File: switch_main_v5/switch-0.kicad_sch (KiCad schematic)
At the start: 43 parts, among them U902 SJA1105QELY, Y902 XRCGB25M000F3A16R0

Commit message: Updated 1v0_buck_converter feedback resistors
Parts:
- removed C937, C938, C939, C941, C942, C943, C944, C945, C961, C967: 1u, Capacitor_SMD:C_0402_1005Metric, symbol Device:C_Small
- removed C940, C946, C947, C948, C949, C950, C951, C952, C953, C954, C955, C956, C957, C958, C959, C960, C962, C963, C964, C965, C966, C968, C969, C970: 100n, Capacitor_SMD:C_0402_1005Metric, symbol Device:C_Small
- removed R904, R906: 10k, Resistor_SMD:R_0402_1005Metric, symbol Device:R_Small
- removed R905: 22R, Resistor_SMD:R_0402_1005Metric, symbol Device:R_Small
- removed TP903, TP904: 1.5mm, TestPoint:TestPoint_Pad_D1.5mm, symbol Connector:TestPoint_Small
- removed U902: SJA1105QELY, project_footprints:BGA159C80P14X14_1200X1200X150, symbol ETH-SWCH:SJA1105QELY
- added C901, C902, C903, C905, C906, C907, C908, C909, C925, C931: 1u, Capacitor_SMD:C_0402_1005Metric, symbol Device:C_Small
- added C904, C910, C911, C912, C913, C914, C915, C916, C917, C918, C919, C920, C921, C922, C923, C924, C926, C927, C928, C929, C930, C932, C933, C934: 100n, Capacitor_SMD:C_0402_1005Metric, symbol Device:C_Small
- added R901, R903: 10k, Resistor_SMD:R_0402_1005Metric, symbol Device:R_Small
- added R902: 22R, Resistor_SMD:R_0402_1005Metric, symbol Device:R_Small
- added TP901, TP902: 1.5mm, TestPoint:TestPoint_Pad_D1.5mm, symbol Connector:TestPoint_Small
- added U901: SJA1105QELY, project_footprints:BGA159C80P14X14_1200X1200X150, symbol ETH-SWCH:SJA1105QELY
- renumbered C971 to C935, C972 to C936, Y902 to Y901
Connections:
- net +1V2: now also C901.1, C903.1, C904.1, C911.1, C912.1, C919.1, C925.1, C926.1, C927.1, C928.1, C929.1, C930.1, C932.1, U901.D6 (VDD_CORE_1), U901.D9 (VDD_CORE_2), U901.F11 (VDD_CORE_4), U901.F4 (VDD_CORE_3), U901.J1 (VDDA_PLL), U901.J11 (VDD_CORE_6), U901.J4 (VDD_CORE_5), U901.K1 (VDDA_OSC), U901.L6 (VDD_CORE_7), U901.L9 (VDD_CORE_8)
- net +1V8: now also C905.1, C906.1, C907.1, C913.1, C914.1, C915.1, C920.1, C921.1, C922.1, C931.1, C933.1, C934.1, U901.D10 (VDDIO_MII2_1), U901.D11 (VDDIO_MII2_2), U901.D4 (VDDIO_MII0_1), U901.D5 (VDDIO_MII1_1), U901.D7 (VDDIO_MII1_2), U901.D8 (VDDIO_MII1_3), U901.E11 (VDDIO_MII2_3), U901.E4 (VDDIO_MII0_2), U901.G4 (VDDIO_MII0_3), U901.H4 (VDDIO_CLO)
- net +3V3: now also C902.1, C908.1, C909.1, C910.1, C916.1, C917.1, C918.1, C923.1, C924.1, R901.2, R903.2, U901.G11 (VDDIO_MII3_1), U901.H11 (VDDIO_MII3_2), U901.K11 (VDDIO_MII3_3), U901.L10 (VDDIO_MII4_2), U901.L11 (VDDIO_MII4_3), U901.L5 (VDDIO_HOST), U901.L8 (VDDIO_MII4_1)
- net CLK: now also U901.P5 (SCK)
- net CLK_OUT: now also R902.1
- net CS: now also R901.1, U901.N6 (SS_N)
- net GND1: now also C901.2, C902.2, C903.2, C904.2, C905.2, C906.2, C907.2, C908.2, C909.2, C910.2, C911.2, C912.2, C913.2, C914.2, C915.2, C916.2, C917.2, C918.2, C919.2, C920.2, C921.2, C922.2, C923.2, C924.2, C925.2, C926.2, C927.2, C928.2, C929.2, C930.2, C931.2, C932.2, C933.2, C934.2, TP901.1, U901.A1 (VSS_1), U901.A14 (VSS_2), U901.B10 (MII2_RX_ER), U901.B13 (VSS_3), U901.B3 (MII1_RX_ER), U901.E10 (VSS_9), U901.E5 (VSS_4), U901.E6 (VSS_5), U901.E7 (VSS_6), U901.E8 (VSS_7), U901.E9 (VSS_8), U901.F10 (VSS_15), U901.F5 (VSS_10), U901.F6 (VSS_11), U901.F7 (VSS_12), U901.F8 (VSS_13), U901.F9 (VSS_14), U901.G10 (VSS_21), U901.G13 (MII3_RXD3), U901.G5 (VSS_16), U901.G6 (VSS_17), U901.G7 (VSS_18), U901.G8 (VSS_19), U901.G9 (VSS_20), U901.H10 (VSS_27), U901.H14 (MII3_RXD2), U901.H2 (MII0_RX_ER), U901.H5 (VSS_22), U901.H6 (VSS_23), U901.H7 (VSS_24), U901.H8 (VSS_25), U901.H9 (VSS_26), U901.J10 (VSS_33), U901.J13 (MII3_RX_CLK/RXC), U901.J2 (VSSA_PLL), U901.J5 (VSS_28), U901.J6 (VSS_29), U901.J7 (VSS_30), U901.J8 (VSS_31), U901.J9 (VSS_32), U901.K10 (VSS_40), U901.K4 (VSS_34), U901.K5 (VSS_35), U901.K6 (VSS_36), U901.K7 (VSS_37), U901.K8 (VSS_38), U901.K9 (VSS_39), U901.L2 (VSSA_OSC), U901.L4 (I.C.), U901.L7 (VSS_41), U901.N11 (MII4_RXD2), U901.N13 (VSS_43), U901.N2 (VSS_42), U901.P1 (VSS_44), U901.P10 (MII4_RX_CLK/RXC), U901.P12 (MII4_RXD3), U901.P13 (MII4_RX_ER), U901.P14 (VSS_45)
- net MISO: now also U901.P4 (SDO)
- net MOSI: now also U901.N5 (SDI)
- net OSC_IN: now also U901.K2 (OSC_IN)
- net OSC_OUT: now also U901.L1 (OSC_OUT)
- net PTP_CLK: now also U901.N4 (PTP_CLK)
- net R_{CLK_OUT}: now also R902.2, U901.H1 (CLK_OUT)
- net xMII0.RX_CLK: now also U901.E2 (MII0_RX_CLK/RXC)
- net xMII0.RX_CTL: now also U901.G1 (MII0_RX_DV/CRS_DV/RX_CTL)
- net xMII0.RX_D0: now also U901.E1 (MII0_RXD0)
- net xMII0.RX_D1: now also U901.F2 (MII0_RXD1)
- net xMII0.RX_D2: now also U901.F1 (MII0_RXD2)
- net xMII0.RX_D3: now also U901.G2 (MII0_RXD3)
- net xMII0.TX_CLK: now also U901.D1 (MII0_TX_CLK/REF_CLK/TXC)
- net xMII0.TX_CTL: now also U901.D2 (MII0_TX_EN/TX_CTL)
- net xMII0.TX_D0: now also U901.A2 (MII0_TXD0)
- net xMII0.TX_D1: now also U901.B1 (MII0_TXD1)
- net xMII0.TX_D2: now also U901.C2 (MII0_TXD2)
- net xMII0.TX_D3: now also U901.C1 (MII0_TXD3)
- net xMII1.RX_CLK: now also U901.B6 (MII1_RX_CLK/RXC)
- net xMII1.RX_CTL: now also U901.A4 (MII1_RX_DV/CRS_DV/RX_CTL)
- net xMII1.RX_D0: now also U901.A6 (MII1_RXD0)
- net xMII1.RX_D1: now also U901.B5 (MII1_RXD1)
- net xMII1.RX_D2: now also U901.A5 (MII1_RXD2)
- net xMII1.RX_D3: now also U901.B4 (MII1_RXD3)
- net xMII1.TX_CLK: now also U901.A7 (MII1_TX_CLK/REF_CLK/TXC)
- net xMII1.TX_CTL: now also U901.B7 (MII1_TTX_EN/TX_CTL)
- net xMII1.TX_D0: now also U901.B9 (MII1_TXD0)
- net xMII1.TX_D1: now also U901.A9 (MII1_TXD1)
- net xMII1.TX_D2: now also U901.B8 (MII1_TXD2)
- net xMII1.TX_D3: now also U901.A8 (MII1_TXD3)
- net xMII2.RX_CLK: now also U901.B14 (MII2_RX_CLK/RXC)
- net xMII2.RX_CTL: now also U901.A11 (MII2_RX_DV/CRS_DV/RX_CTL)
- net xMII2.RX_D0: now also U901.A13 (MII2_RXD0)
- net xMII2.RX_D1: now also U901.B12 (MII2_RXD1)
- net xMII2.RX_D2: now also U901.A12 (MII2_RXD2)
- net xMII2.RX_D3: now also U901.B11 (MII2_RXD3)
- net xMII2.TX_CLK: now also U901.C14 (MII2_TX_CLK/REF_CLK/TXC)
- net xMII2.TX_CTL: now also U901.C13 (MII2_TX_EN/TX_CTL)
- net xMII2.TX_D0: now also U901.E13 (MII2_TXD0)
- net xMII2.TX_D1: now also U901.E14 (MII2_TXD1)
- net xMII2.TX_D2: now also U901.D13 (MII2_TXD2)
- net xMII2.TX_D3: now also U901.D14 (MII2_TXD3)
- net xMII3.RX_CRS_DV: now also U901.G14 (MII3_RX_DV/CRS_DV/RX_CTL)
- net xMII3.RX_D0: now also U901.J14 (MII3_RXD0)
- net xMII3.RX_D1: now also U901.H13 (MII3_RXD1)
- net xMII3.RX_ER: now also U901.F13 (MII3_RX_ER)
- net xMII3.TX_D0: now also U901.M13 (MII3_TXD0)
- net xMII3.TX_D1: now also U901.M14 (MII3_TXD1)
- net xMII3.TX_EN: now also U901.K13 (MII3_TX_EN/TX_CTL)
- net xMII3_REF_CLK: now also U901.K14 (MII3_TX_CLK/REF_CLK/TXC)
- net xMII4.RX_CRS_DV: now also U901.P9 (MII4_TX_EN/TX_CTL)
- net xMII4.RX_D0: now also U901.P7 (MII4_TXD0)
- net xMII4.RX_D1: now also U901.N7 (MII4_TXD1)
- net xMII4.TX_D0: now also U901.N10 (MII4_RXD0)
- net xMII4.TX_D1: now also U901.P11 (MII4_RXD1)
- net xMII4.TX_EN: now also U901.N12 (MII4_RX_DV/CRS_DV/RX_CTL)
- net xMII4_REF_CLK: now also U901.N9 (MII4_TX_CLK/REF_CLK/TXC)
- net ~{RST}: now also R903.1, TP902.1, U901.P3 (RST_N)

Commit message: Placed most remaining passives and test points
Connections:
- net CS renamed SS
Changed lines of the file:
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@@
-		)
-	)
-	(label "CS"
-		(at 228.6 121.92 0)
-		(effects
-			(font
-				(size 1.27 1.27)
-			)
-			(justify left bottom)
 		)
 	)
@@
 		)
 	)
-	(hierarchical_label "CS"
-		(shape input)
-		(at 220.98 121.92 180)
-		(effects
-			(font
-				(size 1.27 1.27)
-			)
-			(justify right)
-		)
-	)
 	(hierarchical_label "xMII4_REF_CLK"
 		(shape output)
@@
 		)
 	)
+	(hierarchical_label "SS"
+		(shape input)
+		(at 220.98 121.92 180)
+		(effects
+			(font
+				(size 1.27 1.27)
+			)
+			(justify right)
+		)
+	)

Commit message: Tidied schematic and PCB
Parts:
- renumbered C901 to C1501, C904 to C1502, C912 to C1503, C919 to C1504, C926 to C1505, C928 to C1506, C929 to C1507, C930 to C1508, C932 to C1509, C905 to C1510, C913 to C1511, C920 to C1512, C906 to C1513, C914 to C1514, C921 to C1515, C907 to C1516, C915 to C1517, C922 to C1518, C935 to C1519, C908 to C1520, C916 to C1521, C923 to C1522, C936 to C1523, C909 to C1524, C917 to C1525, C924 to C1526, C902 to C1527, C910 to C1528, C918 to C1529, C903 to C1530, C911 to C1531, C925 to C1532, C927 to C1533, C931 to C1534, C933 to C1535, C934 to C1536, R901 to R1501, R903 to R1502, R902 to R1503, TP901 to TP1501, TP902 to TP1502, U901 to U1501, Y901 to Y1501

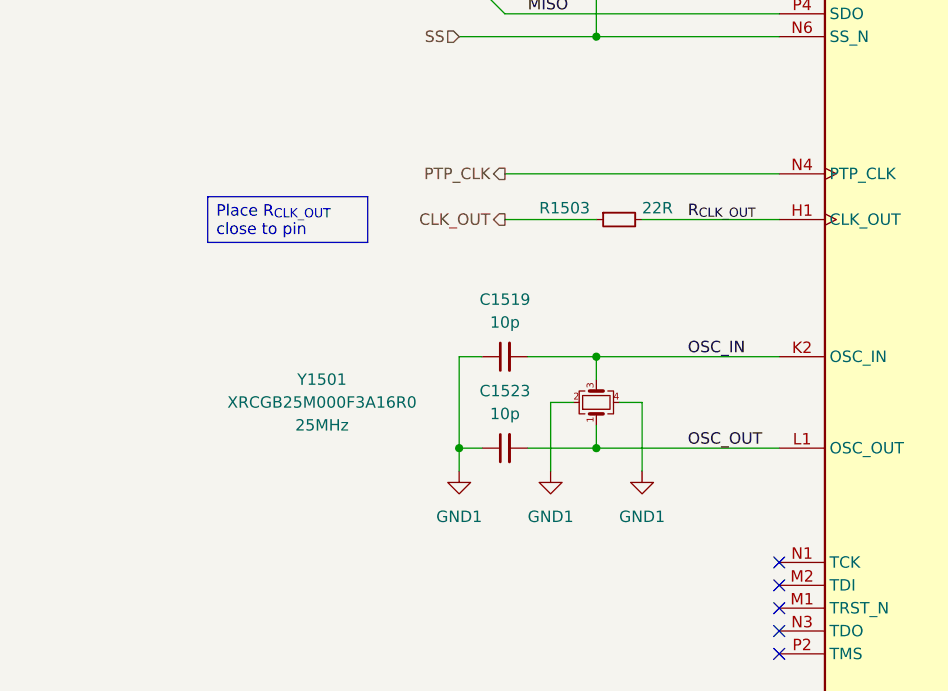
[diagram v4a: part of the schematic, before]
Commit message: Removed one switch crystal so both are now clocked from the same source and timestamps won't drift
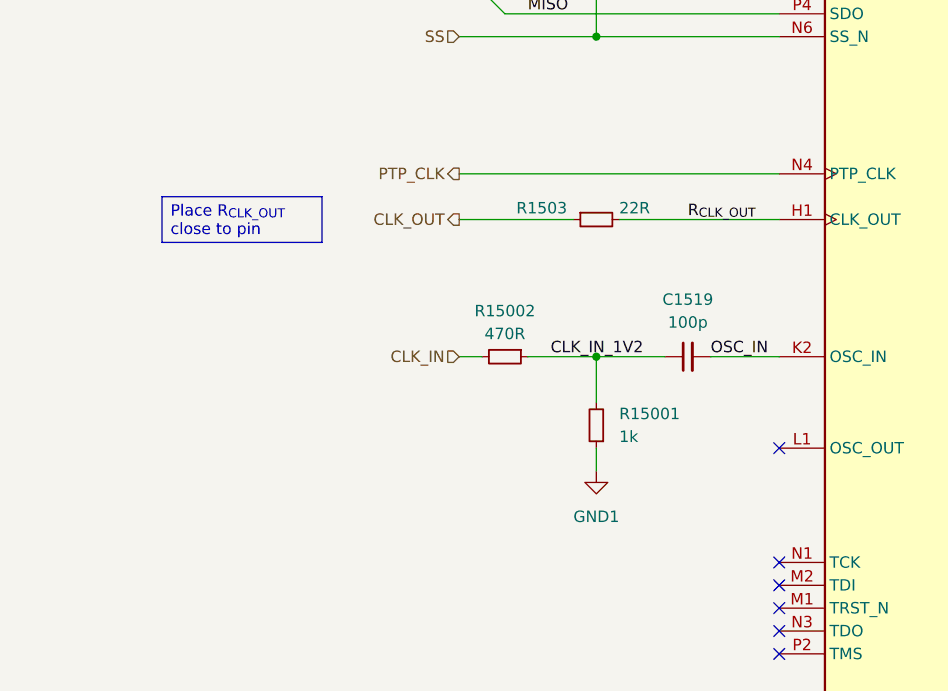
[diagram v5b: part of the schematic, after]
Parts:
- removed C1523: 10p, Capacitor_SMD:C_0402_1005Metric, symbol Device:C_Small
- removed Y1501: XRCGB25M000F3A16R0, project_footprints:XRCGB25M000F3A16R0, symbol Device:Crystal_GND24_Small
- added R15001: 1k, Resistor_SMD:R_0402_1005Metric, symbol Device:R_Small
- added R15002: 470R, Resistor_SMD:R_0402_1005Metric, symbol Device:R_Small
- C1519: value 10p -> 100p
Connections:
- net GND1: now also R15001.1; no longer C1519.1
- net OSC_OUT: no longer names the net of U1501.L1 (OSC_OUT)
- new net CLK_IN: R15002.2
- new net CLK_IN_1V2: C1519.1, R15001.2, R15002.1
- no-connect marks 14 -> 15
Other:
- moved on the sheet: C1519, R1503
